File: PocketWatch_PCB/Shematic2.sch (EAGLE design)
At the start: 57 parts, among them IC1 74HC139D, Q1 BCX71SMD, Q2 BCX71SMD, Q3 BCX71SMD, Q4 BCX71SMD, Q5 BCX70SMD, Q6 BCX70SMD, Q7 BCX70SMD, Q8 BCX70SMD, U2 ATTINY88-AU

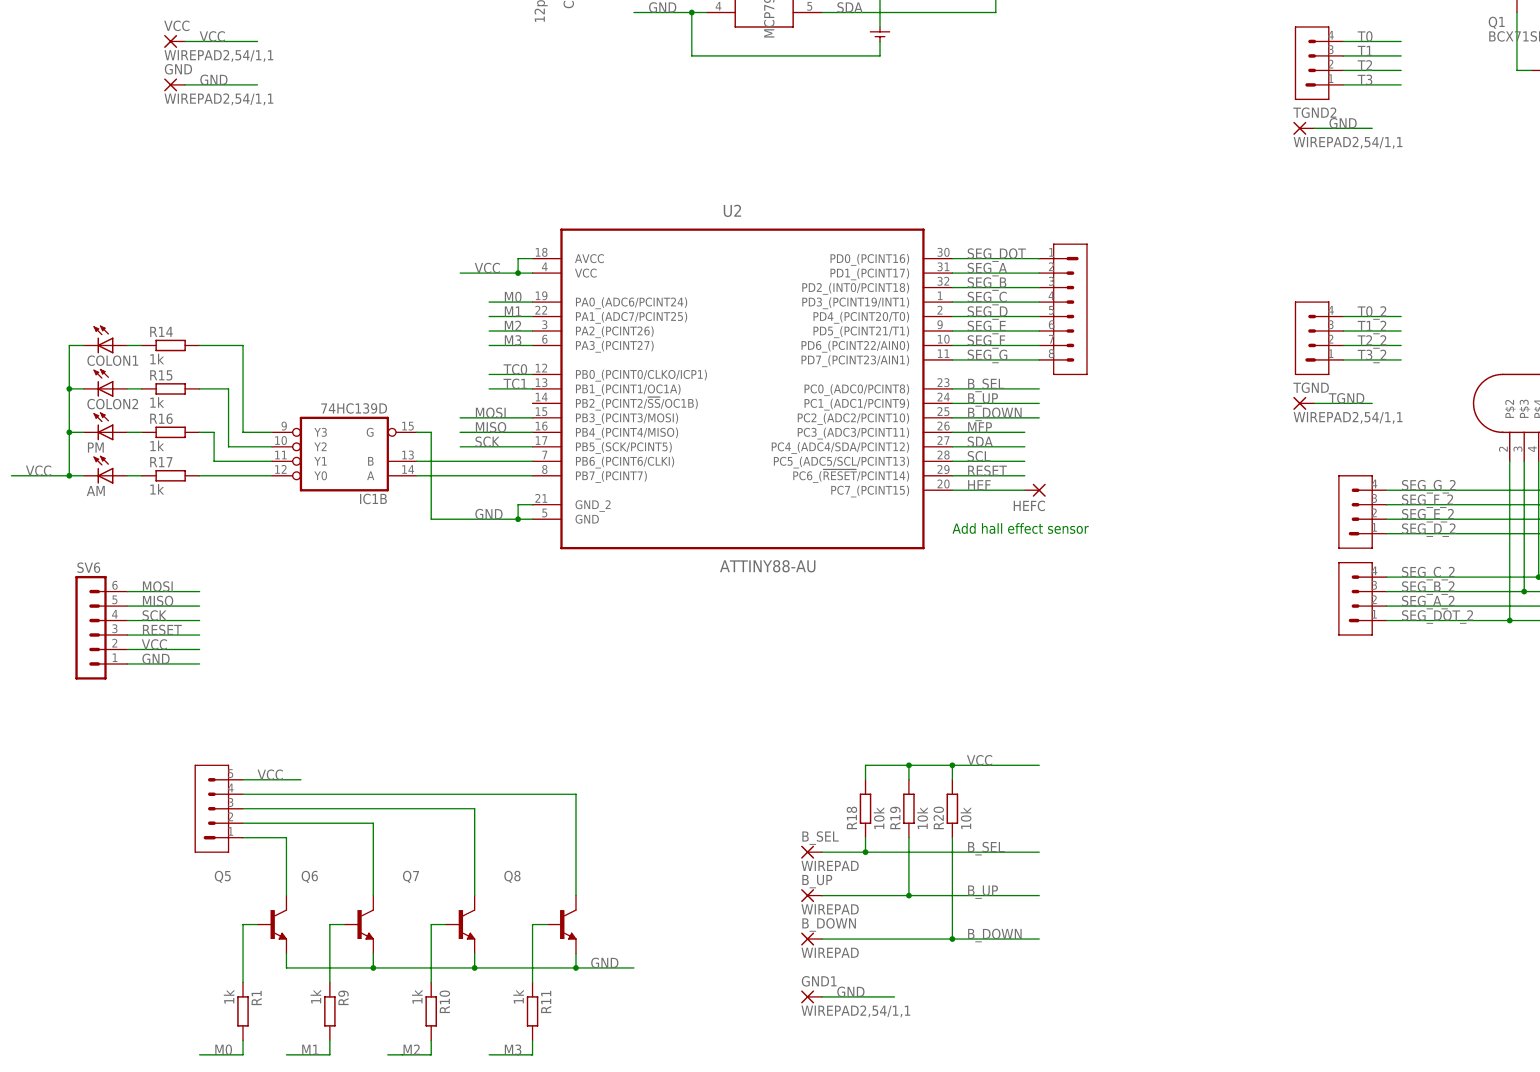
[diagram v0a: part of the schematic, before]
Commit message: Swapped to using stepper motor driver. Routed board
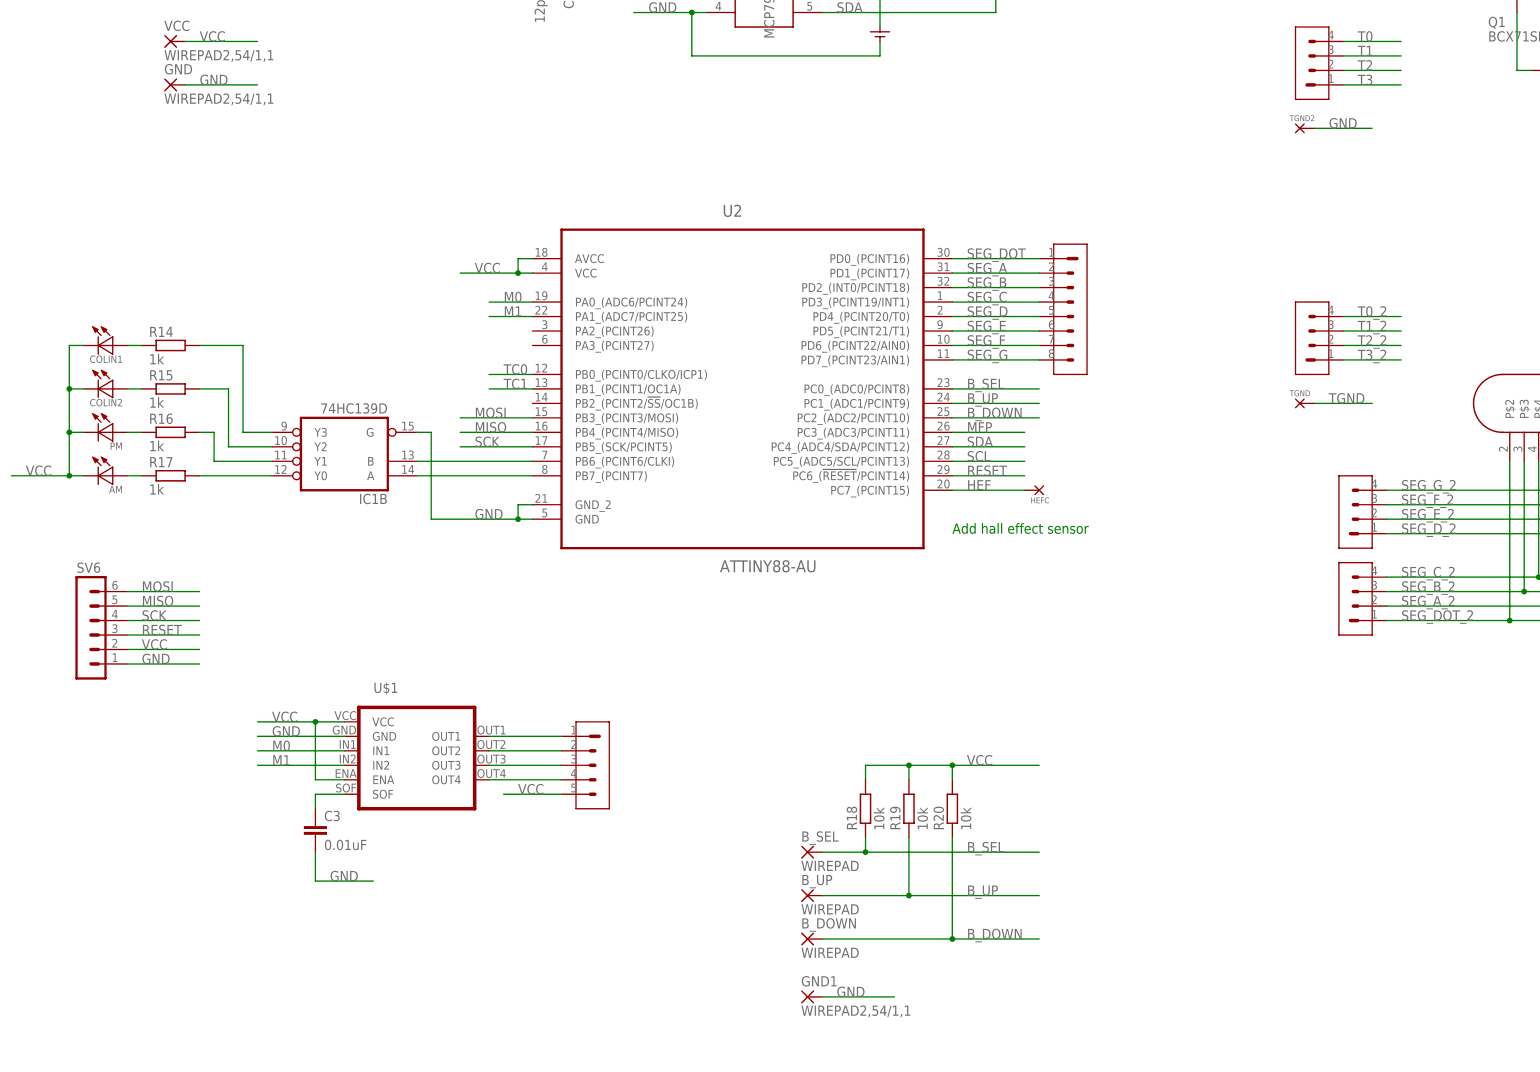
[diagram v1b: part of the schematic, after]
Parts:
- removed COLON1, COLON2: (no value), eagle-ltspice:LED_ELD260
- removed Q5, Q6, Q7, Q8: BCX70SMD, transistor-npn:BCX70SMD
- removed R1, R10, R11, R9: 1k, eagle-ltspice:RR1206
- added C3: 0.01uF, eagle-ltspice:CC1206
- added COLIN1, COLIN2: LED, Library:LED
- added U$1: LB1848MC, Library:LB1848MC
- AM, PM: value (none) -> LED; device eagle-ltspice:LED_ELD260 -> Library:LED
- HEFC, TGND, TGND2: value WIREPAD2,54/1,1 -> H01; device wirepad:WIREPAD2,54/1,1 -> Library:H01
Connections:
- removed net M2: R10.2, U2.PA2_(PCINT26)
- removed net M3: R11.2, U2.PA3_(PCINT27)
- removed net N$23: Q5.B, R1.1
- removed net N$24: Q6.B, R9.1
- removed net N$25: Q7.B, R10.1
- removed net N$26: Q8.B, R11.1
- new net N$31: C3.1, U$1.SOF
- net GND: now also C3.2, TGND2.P$1, U$1.GND; no longer Q5.E, Q6.E, Q7.E, Q8.E, TGND2.P
- net HEF: now also HEFC.P$1; no longer HEFC.P
- net M0: now also U$1.IN1; no longer R1.2
- net M1: now also U$1.IN2; no longer R9.2
- net N$12: now also PM.P$1; no longer PM.A
- net N$14: now also AM.P$1; no longer AM.A
- net N$19: now also SV4.4, U$1.OUT4; no longer Q5.C, SV4.1
- net N$20: now also SV4.3, U$1.OUT3; no longer Q6.C, SV4.2
- net N$21: now also SV4.2, U$1.OUT2; no longer Q7.C, SV4.3
- net N$22: now also SV4.1, U$1.OUT1; no longer Q8.C, SV4.4
- net N$7: now also COLIN1.P$1; no longer COLON1.A
- net N$9: now also COLIN2.P$1; no longer COLON2.A
- net TGND: now also TGND.P$1; no longer TGND.P
- net VCC: now also AM.P$2, COLIN1.P$2, COLIN2.P$2, PM.P$2, U$1.ENA, U$1.VCC; no longer AM.C, COLON1.C, COLON2.C, PM.C
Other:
- moved on the sheet: AM, PM

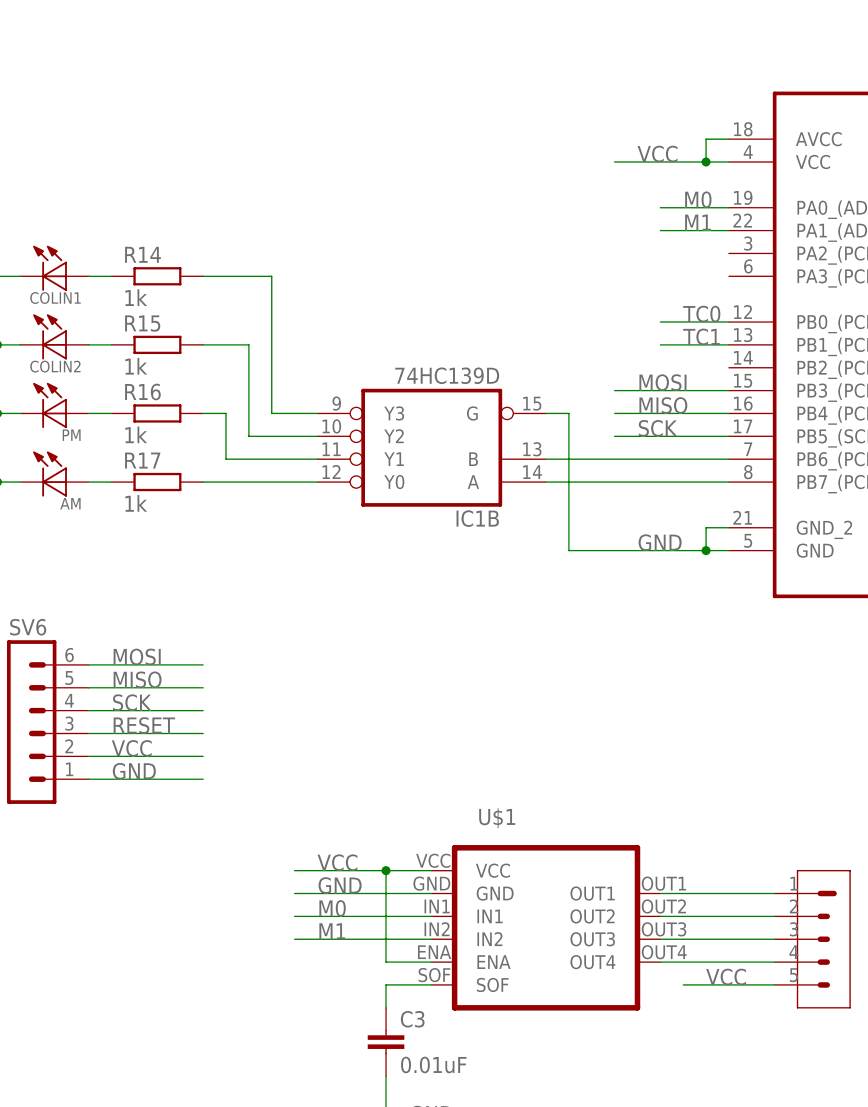
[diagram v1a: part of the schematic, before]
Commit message: Added bypass capacitors. Revised routing.
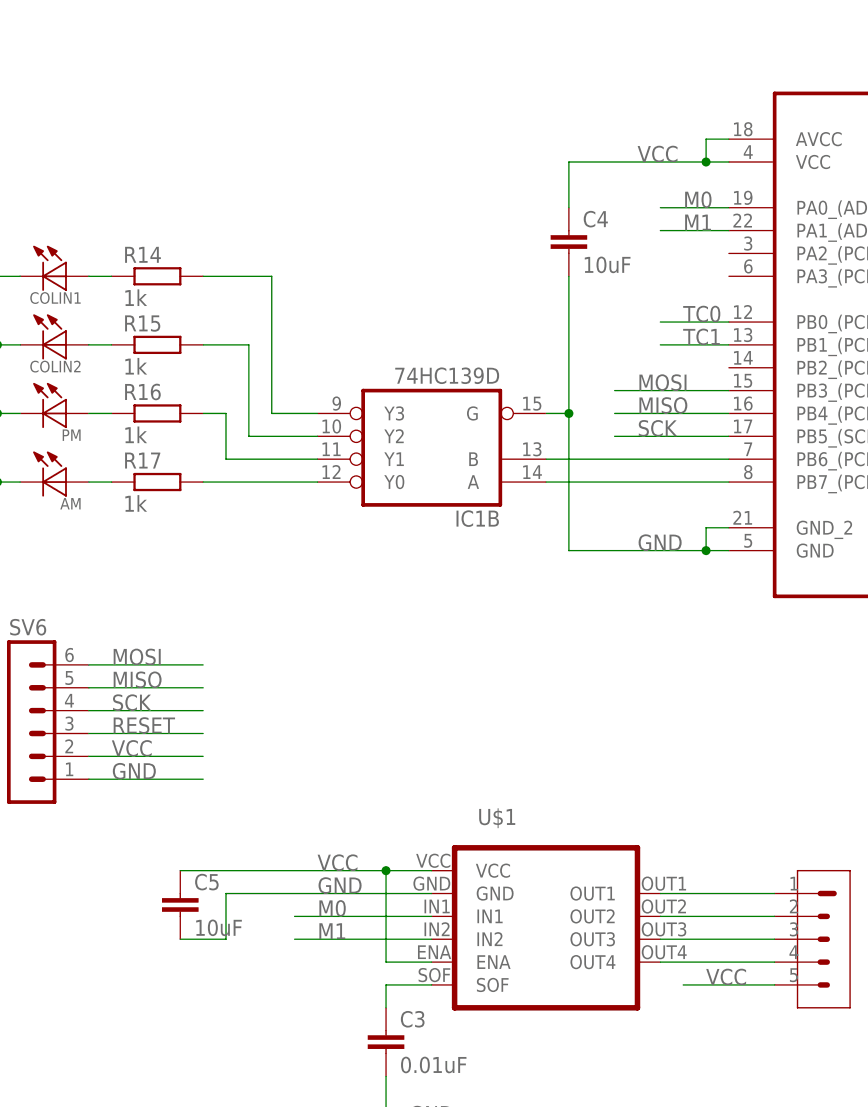
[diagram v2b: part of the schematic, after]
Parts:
- added C4, C5: 10uF, eagle-ltspice:CC1206
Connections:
- net GND: now also C4.2, C5.2
- net VCC: now also C4.1, C5.1
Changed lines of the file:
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@@
 <part name="TGND" library="Library" deviceset="H01" device=""/>
 <part name="TGND2" library="Library" deviceset="H01" device=""/>
+<part name="C4" library="eagle-ltspice" library_urn="urn:adsk.eagle:library:217" deviceset="C" device="C1206" package3d_urn="urn:adsk.eagle:package:13279/1" value="10uF"/>
+<part name="C5" library="eagle-ltspice" library_urn="urn:adsk.eagle:library:217" deviceset="C" device="C1206" package3d_urn="urn:adsk.eagle:package:13279/1" value="10uF"/>
 </parts>
 <sheets>
@@
 <instance part="TGND" gate="G$1" x="162.56" y="-7.62"/>
 <instance part="TGND2" gate="G$1" x="162.56" y="40.64"/>
+<instance part="C4" gate="G$1" x="10.16" y="7.62"/>
+<instance part="C5" gate="G$1" x="-33.02" y="-66.04"/>
 </instances>
 <busses>
@@
 <wire x1="7.62" y1="-12.7" x2="10.16" y2="-12.7" width="0.1524" layer="91"/>
 <wire x1="10.16" y1="-12.7" x2="10.16" y2="-27.94" width="0.1524" layer="91"/>
+<pinref part="C4" gate="G$1" pin="2"/>
+<wire x1="10.16" y1="2.54" x2="10.16" y2="-12.7" width="0.1524" layer="91"/>
+<junction x="10.16" y="-12.7"/>
 </segment>
 <segment>
@@
 <segment>
 <pinref part="U$1" gate="G$1" pin="GND"/>
-<wire x1="-5.08" y1="-66.04" x2="-20.32" y2="-66.04" width="0.1524" layer="91"/>
+<wire x1="-5.08" y1="-66.04" x2="-27.94" y2="-66.04" width="0.1524" layer="91"/>
 <label x="-17.78" y="-66.04" size="1.778" layer="95"/>
+<wire x1="-27.94" y1="-66.04" x2="-27.94" y2="-71.12" width="0.1524" layer="91"/>
+<pinref part="C5" gate="G$1" pin="2"/>
+<wire x1="-27.94" y1="-71.12" x2="-33.02" y2="-71.12" width="0.1524" layer="91"/>
 </segment>
 </net>
@@
 <pinref part="U2" gate="A" pin="VCC"/>
 <wire x1="25.4" y1="15.24" x2="27.94" y2="15.24" width="0.1524" layer="91"/>
-<wire x1="25.4" y1="15.24" x2="15.24" y2="15.24" width="0.1524" layer="91"/>
+<wire x1="25.4" y1="15.24" x2="10.16" y2="15.24" width="0.1524" layer="91"/>
 <junction x="25.4" y="15.24"/>
 <label x="17.78" y="15.24" size="1.778" layer="95"/>
+<pinref part="C4" gate="G$1" pin="1"/>
+<wire x1="10.16" y1="10.16" x2="10.16" y2="15.24" width="0.1524" layer="91"/>
 </segment>
 <segment>
@@
 <wire x1="-5.08" y1="-63.5" x2="-10.16" y2="-63.5" width="0.1524" layer="91"/>
 <pinref part="U$1" gate="G$1" pin="ENA"/>
-<wire x1="-10.16" y1="-63.5" x2="-20.32" y2="-63.5" width="0.1524" layer="91"/>
 <wire x1="-5.08" y1="-73.66" x2="-10.16" y2="-73.66" width="0.1524" layer="91"/>
 <wire x1="-10.16" y1="-73.66" x2="-10.16" y2="-63.5" width="0.1524" layer="91"/>
 <junction x="-10.16" y="-63.5"/>
 <label x="-17.78" y="-63.5" size="1.778" layer="95"/>
-</segment>
-</net>
+<pinref part="C5" gate="G$1" pin="1"/>
+<wire x1="-33.02" y1="-63.5" x2="-10.16" y2="-63.5" width="0.1524" layer="91"/>
+</segment>
+</net>
